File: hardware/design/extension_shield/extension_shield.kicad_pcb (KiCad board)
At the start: 2 copper layers, 118 x 55 mm, 45 parts, among them J1 SSQ-108-XX-X-D, J10 Conn_01x02_Socket, J11 Conn_01x02_Socket, J12 Conn_01x02_Socket, J2 SSQ-110-03-T-D, J3 SSQ-108-XX-X-D, J4 SSQ-106-03-T-D, J5 Conn_01x02_Socket, J6 Conn_01x02_Socket, J7 Conn_01x05_Socket, J8 SSQ-114-03-T-D, J9 SSQ-116-XX-X-D, Q1 BC546, Q2 BC546, Q3 BC546, Q4 BC546, Q5 BC546, U1 DS3231M

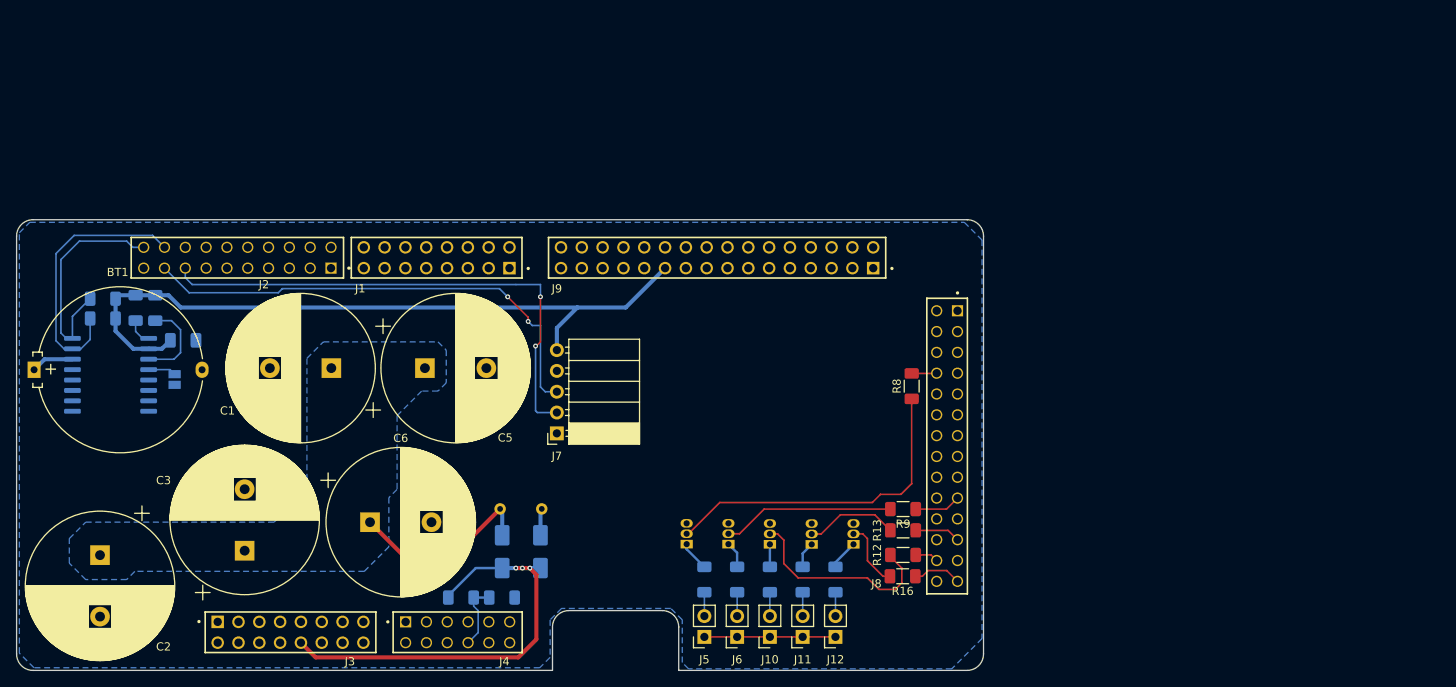
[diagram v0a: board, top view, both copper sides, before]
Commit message: [HW/SHIELD] Adds Genereated PDF Schematic & Newer Version of Expansion Shield.
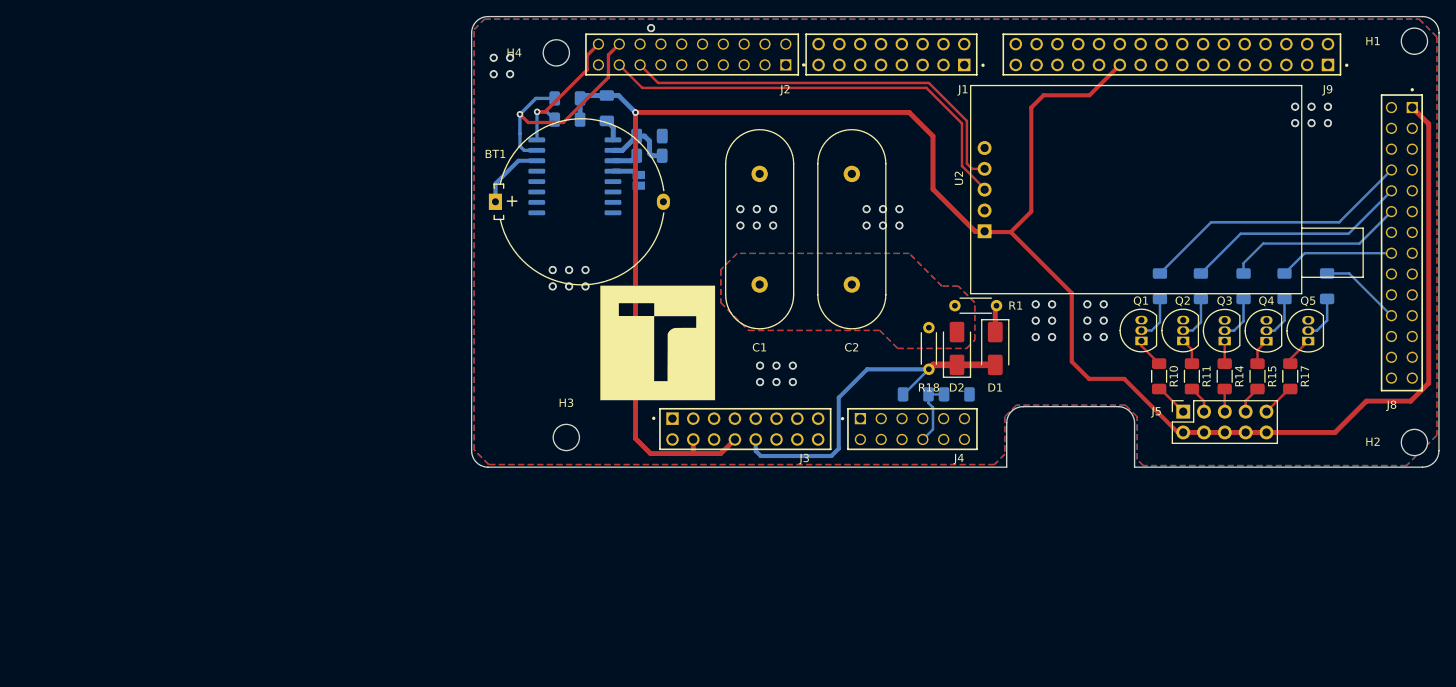
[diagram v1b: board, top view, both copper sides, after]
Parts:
- removed C3, C5, C6: 22000uF, Capacitor_THT:CP_Radial_D18.0mm_P7.50mm
- removed J10, J11, J12, J6: Conn_01x02_Socket, Connector_PinSocket_2.54mm:PinSocket_1x02_P2.54mm_Vertical
- removed J7: Conn_01x05_Socket, Connector_PinSocket_2.54mm:PinSocket_1x05_P2.54mm_Horizontal
- added G***: LOGO, LOGO, F.Cu at (103.8, 104.1)
- added H1: MountingHole, MountingHole:MountingHole_3.2mm_M3, F.Cu at (196.2, 67.3)
- added H2: MountingHole, MountingHole:MountingHole_3.2mm_M3, F.Cu at (196.2, 116.3)
- added H3: MountingHole, MountingHole:MountingHole_3.2mm_M3, F.Cu at (92.7, 115.7)
- added H4: MountingHole, MountingHole:MountingHole_3.2mm_M3, F.Cu at (91.4, 68.7)
- added R18: 10R, Resistor_THT:R_Axial_DIN0204_L3.6mm_D1.6mm_P5.08mm_Horizontal, F.Cu at (136.9, 107.3)
- added U2: NEO-7M-MODULE, Neo7M_Module_Lib:Neo-7M-Module, F.Cu at (143.7, 90.5)
- BT1: value Battery_Cell -> RTC_Battery
- C1, C2: value 22000uF -> 0.33F; footprint Capacitor_THT:CP_Radial_D18.0mm_P7.50mm -> SuperCapacitors:C_Radial_D8mm_W24mm_L14mm_P13.5mm
- C4: value C -> 100n
- D1, D2, Q1, Q2, Q3, Q4, Q5, R1, R10, R11, R14, R15, R17: moved to F.Cu
- J1, J3: value SSQ-108-XX-X-D -> SSQ-108-03-T-D
- J5: value Conn_01x02_Socket -> Conn_02x05_Odd_Even; footprint Connector_PinSocket_2.54mm:PinSocket_1x02_P2.54mm_Vertical -> Connector_PinSocket_2.54mm:PinSocket_2x05_P2.54mm_Vertical
- J9: value SSQ-116-XX-X-D -> SSQ-116-03-T-D
- R12, R13, R16, R8, R9: moved to B.Cu
- moved C2 98.7 mm to (127.5, 93.8), turned to 90 degrees
- moved J5 64.6 mm to (167.9, 112.5), turned to 90 degrees
- moved R4 63.1 mm to (102.8, 81.3), turned to 180 degrees
- moved R16 62.7 mm to (185.5, 97.2), turned to -90 degrees
- moved R6 62.7 mm to (92.8, 74.3)
- moved R5 62.5 mm to (97.6, 75.5)
- moved C4 62.1 mm to (102.8, 78.9)
- moved JP1 61.6 mm to (101.5, 84.3)
- moved U1 61.6 mm to (93.7, 83.8)
- moved J1 60.8 mm to (132.3, 68.9)
- moved Q1 60.8 mm to (162.8, 103.9)
- moved Q2 60.8 mm to (167.9, 103.9)
- moved Q4 60.8 mm to (178.1, 103.9)
- moved J3 60.8 mm to (114.5, 114.6)
- moved D1 60.8 mm to (145.0, 104.8)
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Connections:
- net +5v0 renamed +5V
- net 5v-9v-IN renamed 5V-9V-IN
- net Net-(BT1-+) renamed +BATT
- net P0-10/P2-4 renamed P0-10
- net P0-19/TSI0_CH14 renamed P0-19
- net P0-24/FC1-SDO renamed P0-24
- net P0-25/FC1-SCK renamed P0-25
- net P0-26/FC1-SDI renamed P0-26
- net P0-27/FC1-CS1 renamed P0-27
- net P0-30/P4-13 renamed P0-30
- net P0-3/P5_5 renamed P0-3
- net P1-22/ENC_A renamed P1-22
- net P1-23/P2-6 renamed P1-23
- net P1-2/P2-3 renamed P1-2
- net P1_12/TSI0_CH21 renamed P1_12
- net P2-0/ENC_B renamed P2-0
- net P2-2/PWM1_A2 renamed P2-2
- net P2-3/PWM1_B2 renamed P2-3
- net P2-4/PWM1_A1 renamed P2-4
- net P2-5/PWM1_B1 renamed P2-5
- net P2-6/PWM1_A0 renamed P2-6
- net P2-7/PWM1_B0 renamed P2-7
- net P3-16/P4-5 renamed P3-16
- net P3-17/P4-13 renamed P4-13
- net P3-17/SAI1_TX_FS renamed P3-17
- net P3-18/SAI1_RX_BLCK renamed P3-18
- net P3-19/SAI1_RX_FS renamed P3-19
- net P3-20/SAI1_TXD0 renamed P3-20
- net P3-21/SAI1_RXD0 renamed P3-21
- net P4-0/P1-16 renamed P4-0
- net P4-1/P1-17 renamed P4-1
- net P4-2/TXD2 renamed P4-2
- net P4-3/RXD2 renamed P4-3
- net P5-2/P0-14 renamed P5-2
- net P5-3/P0-22 renamed P5-3
- C4 pad 1: +3v3 -> +3V3
- J1 pad 07: P1-21/SAI1_MCLK -> P1-21
- J1 pad 12: P1-21/P2-7 -> P1-21
- J2 pad 15: P1-1/TSI0_CH1 -> P1-1
- J2 pad 17: P1-0/TSI0_CH0 -> P1-0
- J3 pad 04: +3v3 -> +3V3
- J3 pad 08: +3v3 -> +3V3
- J5 pad 1: +3v3 -> /control_diods/LED_Q1
- J5 pad 2: Net-(J5-Pin_2) -> +3V3
- J8 pad 01: +3v3 -> +3V3
- J9 pad 21: +3v3 -> +3V3
- R10 pad 2: Net-(J5-Pin_2) -> /control_diods/LED_Q1
- R11 pad 2: Net-(J6-Pin_2) -> /control_diods/LED_Q2
- R13 pad 1: P0-9/WR -> P2-11/D3
- R14 pad 2: Net-(J10-Pin_2) -> /control_diods/LED_Q3
- R15 pad 2: Net-(J11-Pin_2) -> /control_diods/LED_Q4
- R16 pad 1: P2-11/D3 -> P4-17/D9
- R17 pad 2: Net-(J12-Pin_2) -> /control_diods/LED_Q5
- R4 pad 1: +3v3 -> +3V3
- R5 pad 1: +3v3 -> +3V3
- R6 pad 1: +3v3 -> +3V3
- R7 pad 1: +3v3 -> +3V3
- R8 pad 1: P4-17/D9 -> P0-7/DC
- R9 pad 1: P0-7/DC -> P0-9/WR
- U1 pad 2: +3v3 -> +3V3
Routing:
- net +3V3: track 0.00 -> 264.8 mm, vias 0 -> 1
- net +3v3: track 104.0 -> 0.00 mm
- net P1-1/TSI0_CH1: track 63.8 -> 0.00 mm, vias 2 -> 0
- net P1-0/TSI0_CH0: track 59.2 -> 0.00 mm, vias 2 -> 0
- net P1-0: track 0.00 -> 54.0 mm
- net P1-1: track 0.00 -> 50.3 mm
- net Net-(Q1-B): track 40.3 -> 5.53 mm
- net P0-7/DC: track 3.07 -> 33.5 mm
- net P0-9/WR: track 0.00 -> 27.4 mm
- net Net-(D2-A): track 23.1 -> 0.00 mm
- net P0-13/TE: track 0.00 -> 21.9 mm
- net Net-(Q3-B): track 24.9 -> 5.50 mm
- net Net-(Q2-B): track 21.0 -> 5.43 mm
- net P2-11/D3: track 0.00 -> 14.1 mm
- net +5V: track 54.0 -> 43.6 mm, vias 3 -> 0
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- added copper zone on F.Cu, net GND
- added copper zone on F.Cu, net Net-(D2-A)
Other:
- board size 118 x 55 mm -> 118.1 x 55 mm
